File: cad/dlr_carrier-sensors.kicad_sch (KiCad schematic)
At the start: 15 parts, among them J10 YL-83, J8 FLIR_LEPTON_FFC, J9 SI1145, U5 DHT22, U6 ADS1115

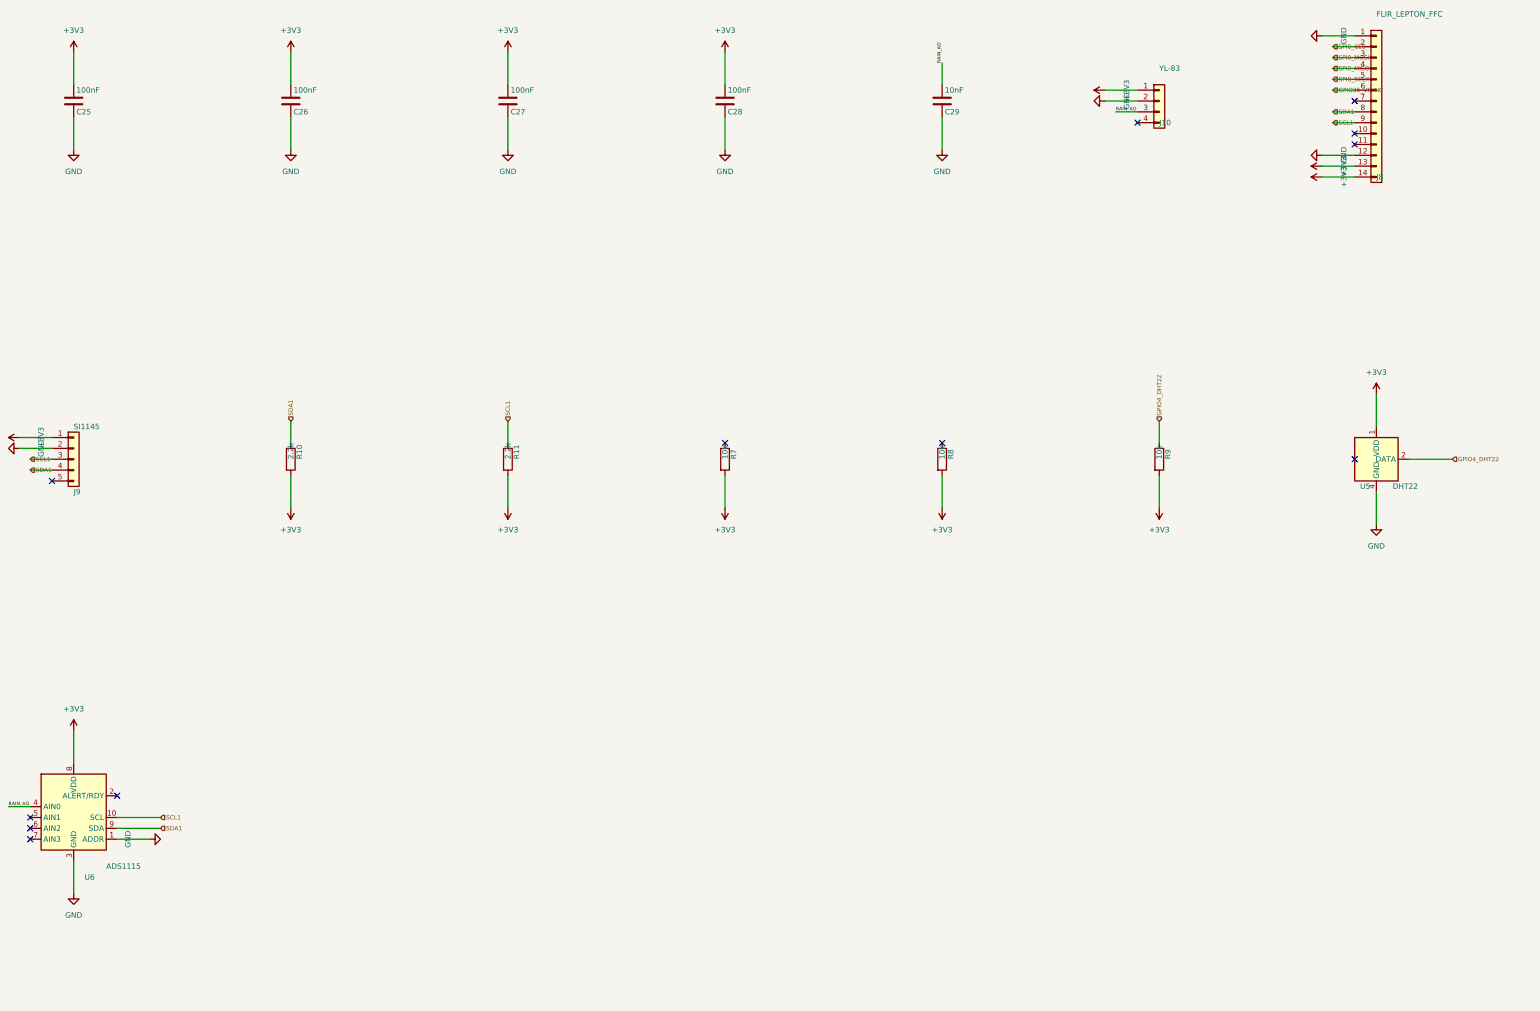
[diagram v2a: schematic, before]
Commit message: 🩺 fix(schematic): match hierarchical label type to the sheet pin
The 117 KiCad 9 errors were a type mismatch, not the hierarchy metadata: every
child hierarchical label was written as `(shape input)` while the root's sheet pins
are bidirectional. KiCad's hier_label_mismatch check compares electrical type as
well as name, so on KiCad 9 every cross-sheet net failed, and the root labels then
read as dangling. KiCad 10 tolerates the mismatch, which is why it passed here.

kicad-sch-api 0.5.6 accepts a shape argument on add_hierarchical_label and ignores
it — the third serialization bug worked around in this generator — so the shape is
rewritten in the saved sheet.

Co-Authored-By: Claude Opus 5 <noreply@anthropic.com>
Claude-Session: https://claude.ai/code/session_011xr7VCL7rkJj2WE2uQF7sF
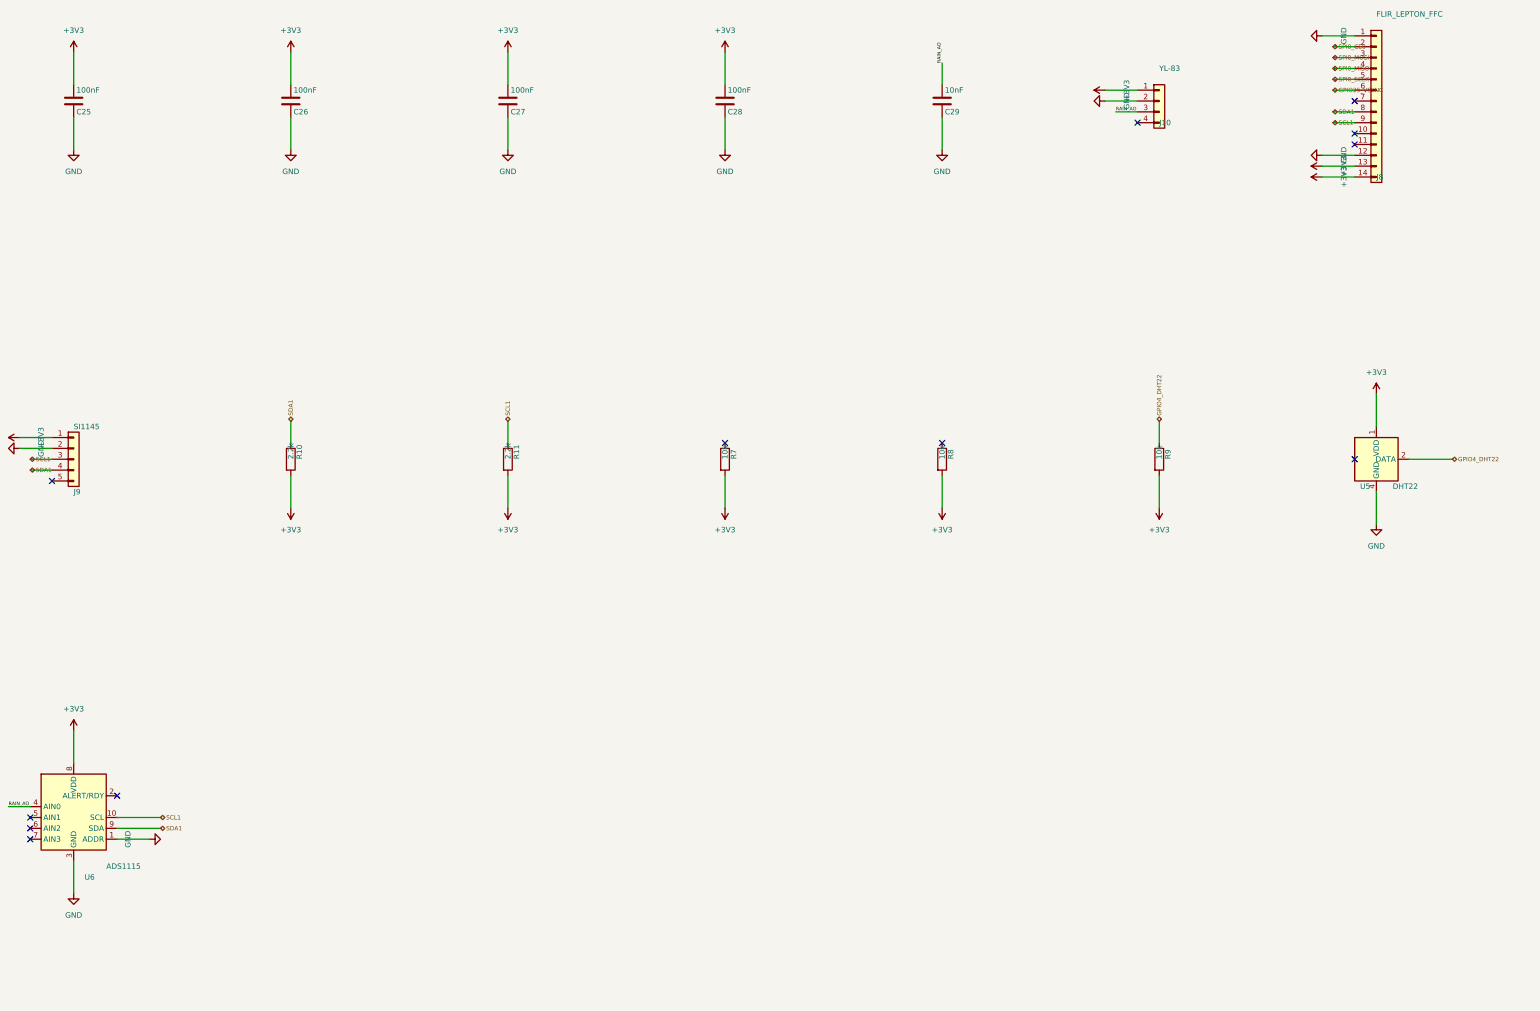
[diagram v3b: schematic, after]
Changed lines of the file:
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@@
 		(instances
 			(project "IEEE 738 SENSORS"
-				(path "/ad58629c-2314-4e8d-95b2-00f0562e8317"
+				(path "/60ce49b7-5723-40b3-8af3-b298ee684017"
 					(reference "C25")
 					(unit 1)
@@
 		(instances
 			(project "IEEE 738 SENSORS"
-				(path "/ad58629c-2314-4e8d-95b2-00f0562e8317"
+				(path "/60ce49b7-5723-40b3-8af3-b298ee684017"
 					(reference "C26")
 					(unit 1)
@@
 		(instances
 			(project "IEEE 738 SENSORS"
-				(path "/ad58629c-2314-4e8d-95b2-00f0562e8317"
+				(path "/60ce49b7-5723-40b3-8af3-b298ee684017"
 					(reference "C27")
 					(unit 1)
@@
 		(instances
 			(project "IEEE 738 SENSORS"
-				(path "/ad58629c-2314-4e8d-95b2-00f0562e8317"
+				(path "/60ce49b7-5723-40b3-8af3-b298ee684017"
 					(reference "C28")
 					(unit 1)
@@
 		(instances
 			(project "IEEE 738 SENSORS"
-				(path "/ad58629c-2314-4e8d-95b2-00f0562e8317"
+				(path "/60ce49b7-5723-40b3-8af3-b298ee684017"
 					(reference "C29")
 					(unit 1)
@@
 		(instances
 			(project "IEEE 738 SENSORS"
-				(path "/ad58629c-2314-4e8d-95b2-00f0562e8317"
+				(path "/60ce49b7-5723-40b3-8af3-b298ee684017"
 					(reference "J10")
 					(unit 1)
@@
 		(instances
 			(project "IEEE 738 SENSORS"
-				(path "/ad58629c-2314-4e8d-95b2-00f0562e8317"
+				(path "/60ce49b7-5723-40b3-8af3-b298ee684017"
 					(reference "J8")
 					(unit 1)
@@
 		(instances
 			(project "IEEE 738 SENSORS"
-				(path "/ad58629c-2314-4e8d-95b2-00f0562e8317"
+				(path "/60ce49b7-5723-40b3-8af3-b298ee684017"
 					(reference "J9")
 					(unit 1)
@@
 		(instances
 			(project "IEEE 738 SENSORS"
-				(path "/ad58629c-2314-4e8d-95b2-00f0562e8317"
+				(path "/60ce49b7-5723-40b3-8af3-b298ee684017"
 					(reference "R10")
 					(unit 1)
@@
 		(instances
 			(project "IEEE 738 SENSORS"
-				(path "/ad58629c-2314-4e8d-95b2-00f0562e8317"
+				(path "/60ce49b7-5723-40b3-8af3-b298ee684017"
 					(reference "R11")
 					(unit 1)
@@
 		(instances
 			(project "IEEE 738 SENSORS"
-				(path "/ad58629c-2314-4e8d-95b2-00f0562e8317"
+				(path "/60ce49b7-5723-40b3-8af3-b298ee684017"
 					(reference "R7")
 					(unit 1)
@@
 		(instances
 			(project "IEEE 738 SENSORS"
-				(path "/ad58629c-2314-4e8d-95b2-00f0562e8317"
+				(path "/60ce49b7-5723-40b3-8af3-b298ee684017"
 					(reference "R8")
 					(unit 1)
@@
 		(instances
 			(project "IEEE 738 SENSORS"
-				(path "/ad58629c-2314-4e8d-95b2-00f0562e8317"
+				(path "/60ce49b7-5723-40b3-8af3-b298ee684017"
 					(reference "R9")
 					(unit 1)
@@
 		(instances
 			(project "IEEE 738 SENSORS"
-				(path "/ad58629c-2314-4e8d-95b2-00f0562e8317"
+				(path "/60ce49b7-5723-40b3-8af3-b298ee684017"
 					(reference "U5")
 					(unit 1)
@@
 		(instances
 			(project "IEEE 738 SENSORS"
-				(path "/ad58629c-2314-4e8d-95b2-00f0562e8317"
+				(path "/60ce49b7-5723-40b3-8af3-b298ee684017"
 					(reference "U6")
 					(unit 1)
@@
 		(instances
 			(project "IEEE 738 SENSORS"
-				(path "/ad58629c-2314-4e8d-95b2-00f0562e8317"
+				(path "/60ce49b7-5723-40b3-8af3-b298ee684017"
 					(reference "#PWR001")
 					(unit 1)
@@
 		(instances
 			(project "IEEE 738 SENSORS"
-				(path "/ad58629c-2314-4e8d-95b2-00f0562e8317"
+				(path "/60ce49b7-5723-40b3-8af3-b298ee684017"
 					(reference "#PWR002")
 					(unit 1)
@@
 		(instances
 			(project "IEEE 738 SENSORS"
-				(path "/ad58629c-2314-4e8d-95b2-00f0562e8317"
+				(path "/60ce49b7-5723-40b3-8af3-b298ee684017"
 					(reference "#PWR003")
 					(unit 1)
@@
 		(instances
 			(project "IEEE 738 SENSORS"
-				(path "/ad58629c-2314-4e8d-95b2-00f0562e8317"
+				(path "/60ce49b7-5723-40b3-8af3-b298ee684017"
 					(reference "#PWR004")
 					(unit 1)
@@
 		(instances
 			(project "IEEE 738 SENSORS"
-				(path "/ad58629c-2314-4e8d-95b2-00f0562e8317"
+				(path "/60ce49b7-5723-40b3-8af3-b298ee684017"
 					(reference "#PWR005")
 					(unit 1)
@@
 		(instances
 			(project "IEEE 738 SENSORS"
-				(path "/ad58629c-2314-4e8d-95b2-00f0562e8317"
+				(path "/60ce49b7-5723-40b3-8af3-b298ee684017"
 					(reference "#PWR006")
 					(unit 1)
@@
 		(instances
 			(project "IEEE 738 SENSORS"
-				(path "/ad58629c-2314-4e8d-95b2-00f0562e8317"
+				(path "/60ce49b7-5723-40b3-8af3-b298ee684017"
 					(reference "#PWR007")
 					(unit 1)
@@
 		(instances
 			(project "IEEE 738 SENSORS"
-				(path "/ad58629c-2314-4e8d-95b2-00f0562e8317"
+				(path "/60ce49b7-5723-40b3-8af3-b298ee684017"
 					(reference "#PWR008")
 					(unit 1)
@@
 		(instances
 			(project "IEEE 738 SENSORS"
-				(path "/ad58629c-2314-4e8d-95b2-00f0562e8317"
+				(path "/60ce49b7-5723-40b3-8af3-b298ee684017"
 					(reference "#PWR009")
 					(unit 1)
@@
 		(instances
 			(project "IEEE 738 SENSORS"
-				(path "/ad58629c-2314-4e8d-95b2-00f0562e8317"
+				(path "/60ce49b7-5723-40b3-8af3-b298ee684017"
 					(reference "#PWR010")
 					(unit 1)
@@
 		(instances
 			(project "IEEE 738 SENSORS"
-				(path "/ad58629c-2314-4e8d-95b2-00f0562e8317"
+				(path "/60ce49b7-5723-40b3-8af3-b298ee684017"
 					(reference "#PWR011")
 					(unit 1)
@@
 		(instances
 			(project "IEEE 738 SENSORS"
-				(path "/ad58629c-2314-4e8d-95b2-00f0562e8317"
+				(path "/60ce49b7-5723-40b3-8af3-b298ee684017"
 					(reference "#PWR012")
 					(unit 1)
@@
 		(instances
 			(project "IEEE 738 SENSORS"
-				(path "/ad58629c-2314-4e8d-95b2-00f0562e8317"
+				(path "/60ce49b7-5723-40b3-8af3-b298ee684017"
 					(reference "#PWR013")
 					(unit 1)
@@
 		(instances
 			(project "IEEE 738 SENSORS"
-				(path "/ad58629c-2314-4e8d-95b2-00f0562e8317"
+				(path "/60ce49b7-5723-40b3-8af3-b298ee684017"
 					(reference "#PWR014")
 					(unit 1)
@@
 		(instances
 			(project "IEEE 738 SENSORS"
-				(path "/ad58629c-2314-4e8d-95b2-00f0562e8317"
+				(path "/60ce49b7-5723-40b3-8af3-b298ee684017"
 					(reference "#PWR015")
 					(unit 1)
@@
 		(instances
 			(project "IEEE 738 SENSORS"
-				(path "/ad58629c-2314-4e8d-95b2-00f0562e8317"
+				(path "/60ce49b7-5723-40b3-8af3-b298ee684017"
 					(reference "#PWR016")
 					(unit 1)
@@
 		(instances
 			(project "IEEE 738 SENSORS"
-				(path "/ad58629c-2314-4e8d-95b2-00f0562e8317"
+				(path "/60ce49b7-5723-40b3-8af3-b298ee684017"
 					(reference "#PWR017")
 					(unit 1)
@@
 		(instances
 			(project "IEEE 738 SENSORS"
-				(path "/ad58629c-2314-4e8d-95b2-00f0562e8317"
+				(path "/60ce49b7-5723-40b3-8af3-b298ee684017"
 					(reference "#PWR018")
 					(unit 1)
@@
 		(instances
 			(project "IEEE 738 SENSORS"
-				(path "/ad58629c-2314-4e8d-95b2-00f0562e8317"
+				(path "/60ce49b7-5723-40b3-8af3-b298ee684017"
 					(reference "#PWR019")
 					(unit 1)
@@
 		(instances
 			(project "IEEE 738 SENSORS"
-				(path "/ad58629c-2314-4e8d-95b2-00f0562e8317"
+				(path "/60ce49b7-5723-40b3-8af3-b298ee684017"
 					(reference "#PWR020")
 					(unit 1)
@@
 		(instances
 			(project "IEEE 738 SENSORS"
-				(path "/ad58629c-2314-4e8d-95b2-00f0562e8317"
+				(path "/60ce49b7-5723-40b3-8af3-b298ee684017"
 					(reference "#PWR021")
 					(unit 1)
@@
 		(instances
 			(project "IEEE 738 SENSORS"
-				(path "/ad58629c-2314-4e8d-95b2-00f0562e8317"
+				(path "/60ce49b7-5723-40b3-8af3-b298ee684017"
 					(reference "#PWR022")
 					(unit 1)
@@
 		(instances
 			(project "IEEE 738 SENSORS"
-				(path "/ad58629c-2314-4e8d-95b2-00f0562e8317"
+				(path "/60ce49b7-5723-40b3-8af3-b298ee684017"
 					(reference "#PWR023")
 					(unit 1)
@@
 		(instances
 			(project "IEEE 738 SENSORS"
-				(path "/ad58629c-2314-4e8d-95b2-00f0562e8317"
+				(path "/60ce49b7-5723-40b3-8af3-b298ee684017"
 					(reference "#PWR024")
 					(unit 1)
@@
 		(instances
 			(project "IEEE 738 SENSORS"
-				(path "/ad58629c-2314-4e8d-95b2-00f0562e8317"
+				(path "/60ce49b7-5723-40b3-8af3-b298ee684017"
 					(reference "#PWR025")
 					(unit 1)
@@
 		(instances
 			(project "IEEE 738 SENSORS"
-				(path "/ad58629c-2314-4e8d-95b2-00f0562e8317"
+				(path "/60ce49b7-5723-40b3-8af3-b298ee684017"
 					(reference "#PWR026")
 					(unit 1)
@@
 		(instances
 			(project "IEEE 738 SENSORS"
-				(path "/ad58629c-2314-4e8d-95b2-00f0562e8317"
+				(path "/60ce49b7-5723-40b3-8af3-b298ee684017"
 					(reference "#PWR027")
 					(unit 1)
@@
 	)
 	(hierarchical_label "GPIO25_VSYNC"
-		(shape input)
+		(shape bidirectional)
 		(at 358.14 77.47 180)
 		(effects
@@
 	)
 	(hierarchical_label "GPIO4_DHT22"
-		(shape input)
+		(shape bidirectional)
 		(at 317.5 154.94 90)
 		(effects
@@
 	)
 	(hierarchical_label "GPIO4_DHT22"
-		(shape input)
+		(shape bidirectional)
 		(at 386.08 163.83 0)
 		(effects
@@
 	)
 	(hierarchical_label "SCL1"
-		(shape input)
+		(shape bidirectional)
 		(at 358.14 85.09 180)
 		(effects
@@
 	)
 	(hierarchical_label "SCL1"
-		(shape input)
+		(shape bidirectional)
 		(at 53.34 163.83 180)
 		(effects
@@
 	)
 	(hierarchical_label "SCL1"
-		(shape input)
+		(shape bidirectional)
 		(at 165.1 154.94 90)
 		(effects
@@
 	)
 	(hierarchical_label "SCL1"
-		(shape input)
+		(shape bidirectional)
 		(at 83.82 247.65 0)
 		(effects
@@
 	)
 	(hierarchical_label "SDA1"
-		(shape input)
+		(shape bidirectional)
 		(at 358.14 82.55 180)
 		(effects
@@
 	)
 	(hierarchical_label "SDA1"
-		(shape input)
+		(shape bidirectional)
 		(at 53.34 166.37 180)
 		(effects
@@
 	)
 	(hierarchical_label "SDA1"
-		(shape input)
+		(shape bidirectional)
 		(at 114.3 154.94 90)
 		(effects
@@
 	)
 	(hierarchical_label "SDA1"
-		(shape input)
+		(shape bidirectional)
 		(at 83.82 250.19 0)
 		(effects
@@
 	)
 	(hierarchical_label "SPI0_CE0"
-		(shape input)
+		(shape bidirectional)
 		(at 358.14 67.31 180)
 		(effects
@@
 	)
 	(hierarchical_label "SPI0_MISO"
-		(shape input)
+		(shape bidirectional)
 		(at 358.14 72.39 180)
 		(effects
@@
 	)
 	(hierarchical_label "SPI0_MOSI"
-		(shape input)
+		(shape bidirectional)
 		(at 358.14 69.85 180)
 		(effects
@@
 	)
 	(hierarchical_label "SPI0_SCLK"
-		(shape input)
+		(shape bidirectional)
 		(at 358.14 74.93 180)
 		(effects
@@
 	)
 	(sheet_instances
-		(path "/32a8a524-8308-4327-a4c2-fe779a71d0ce"
+		(path "/6ec6768b-b569-4381-8a3d-e6e832fe942c"
 			(page "5")
 		)

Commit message: 🩺 refactor(schematic): cross-sheet nets via global labels, no sheet pins
Three attempts at making the hierarchical sheet-pin mechanism pass KiCad 9 failed
(project name, instance paths, label type), so the mechanism goes. Cross-sheet nets
now connect by name through global labels on the child sheets; the root carries
sheet symbols only — no pins, no stub wires, no labels.

That removes the whole hier_label_mismatch / label_dangling class rather than
chasing it, and it matches the connectivity style the generate-schematic skill
already prescribes for this project ("all inter-block connections use net labels").

kicad-sch-api's add_global_label still does not serialize, so the labels are emitted
as hierarchical and rewritten in the saved sheet.

Co-Authored-By: Claude Opus 5 <noreply@anthropic.com>
Claude-Session: https://claude.ai/code/session_011xr7VCL7rkJj2WE2uQF7sF
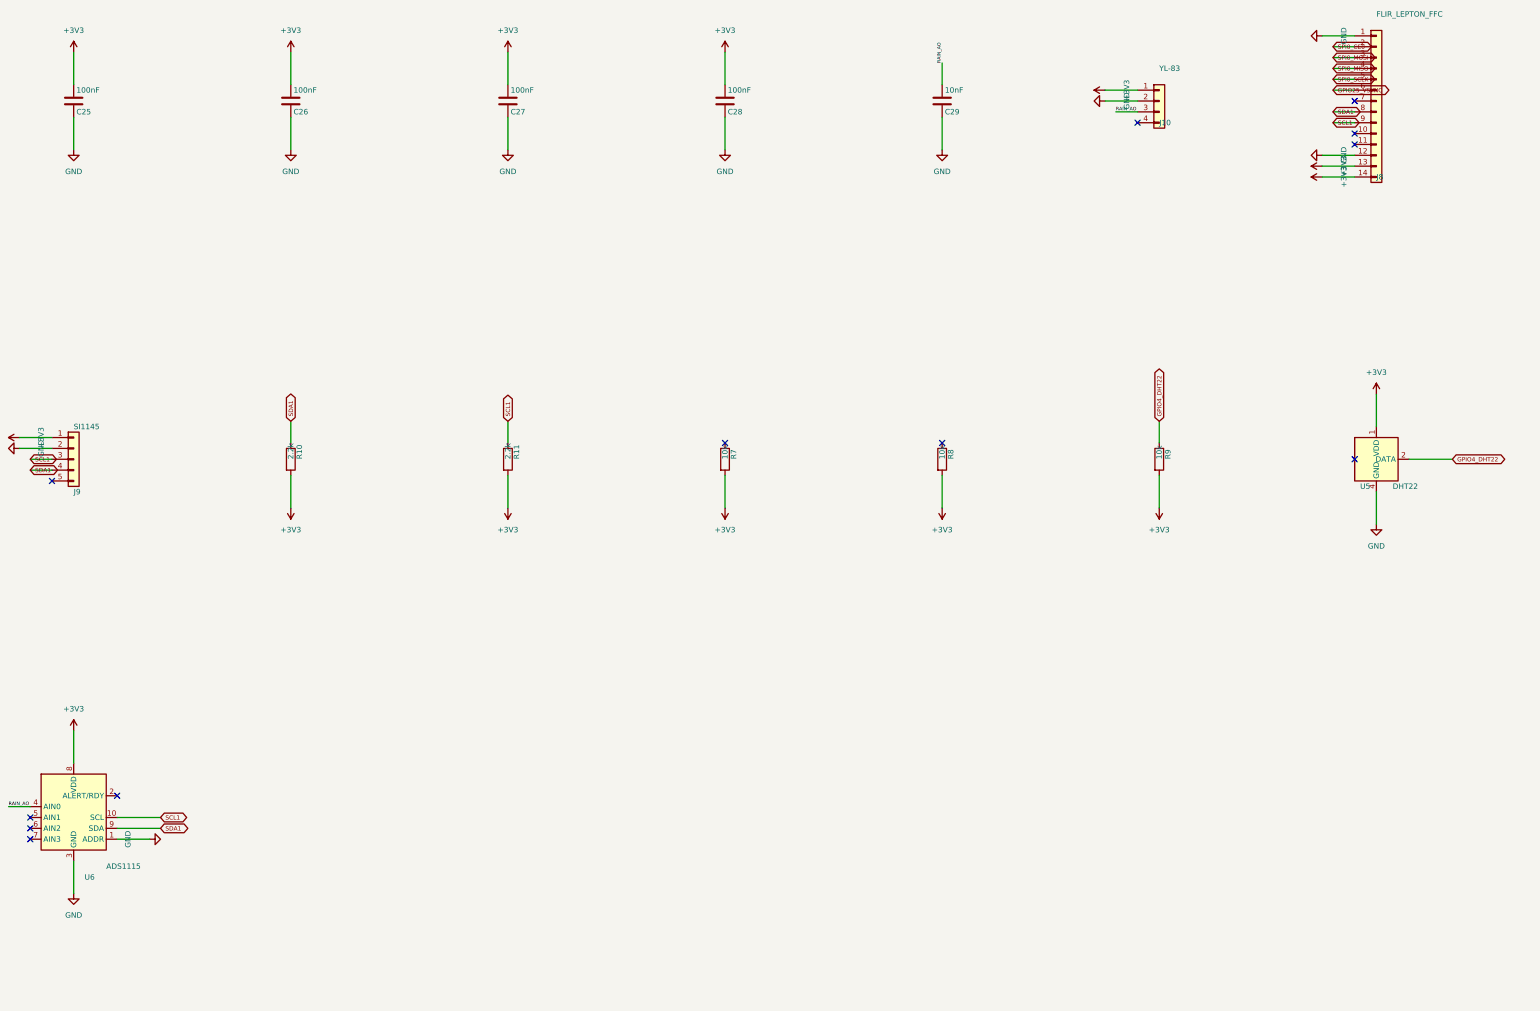
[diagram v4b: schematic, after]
